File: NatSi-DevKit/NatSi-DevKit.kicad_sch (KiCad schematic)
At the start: 42 parts, among them J1 USB_TypeC, J2 Conn_01x22_Pin, J3 Conn_01x22_Pin, J4 MEM2067-02-180-00-A_REVB, SW1 SW_Push, SW2 SW_Push, SW3 SW_Push, U1 USBLC6-2SC6, U2 ESP32-S3-WROOM-1, U3 NCP1117-3.3_SOT223

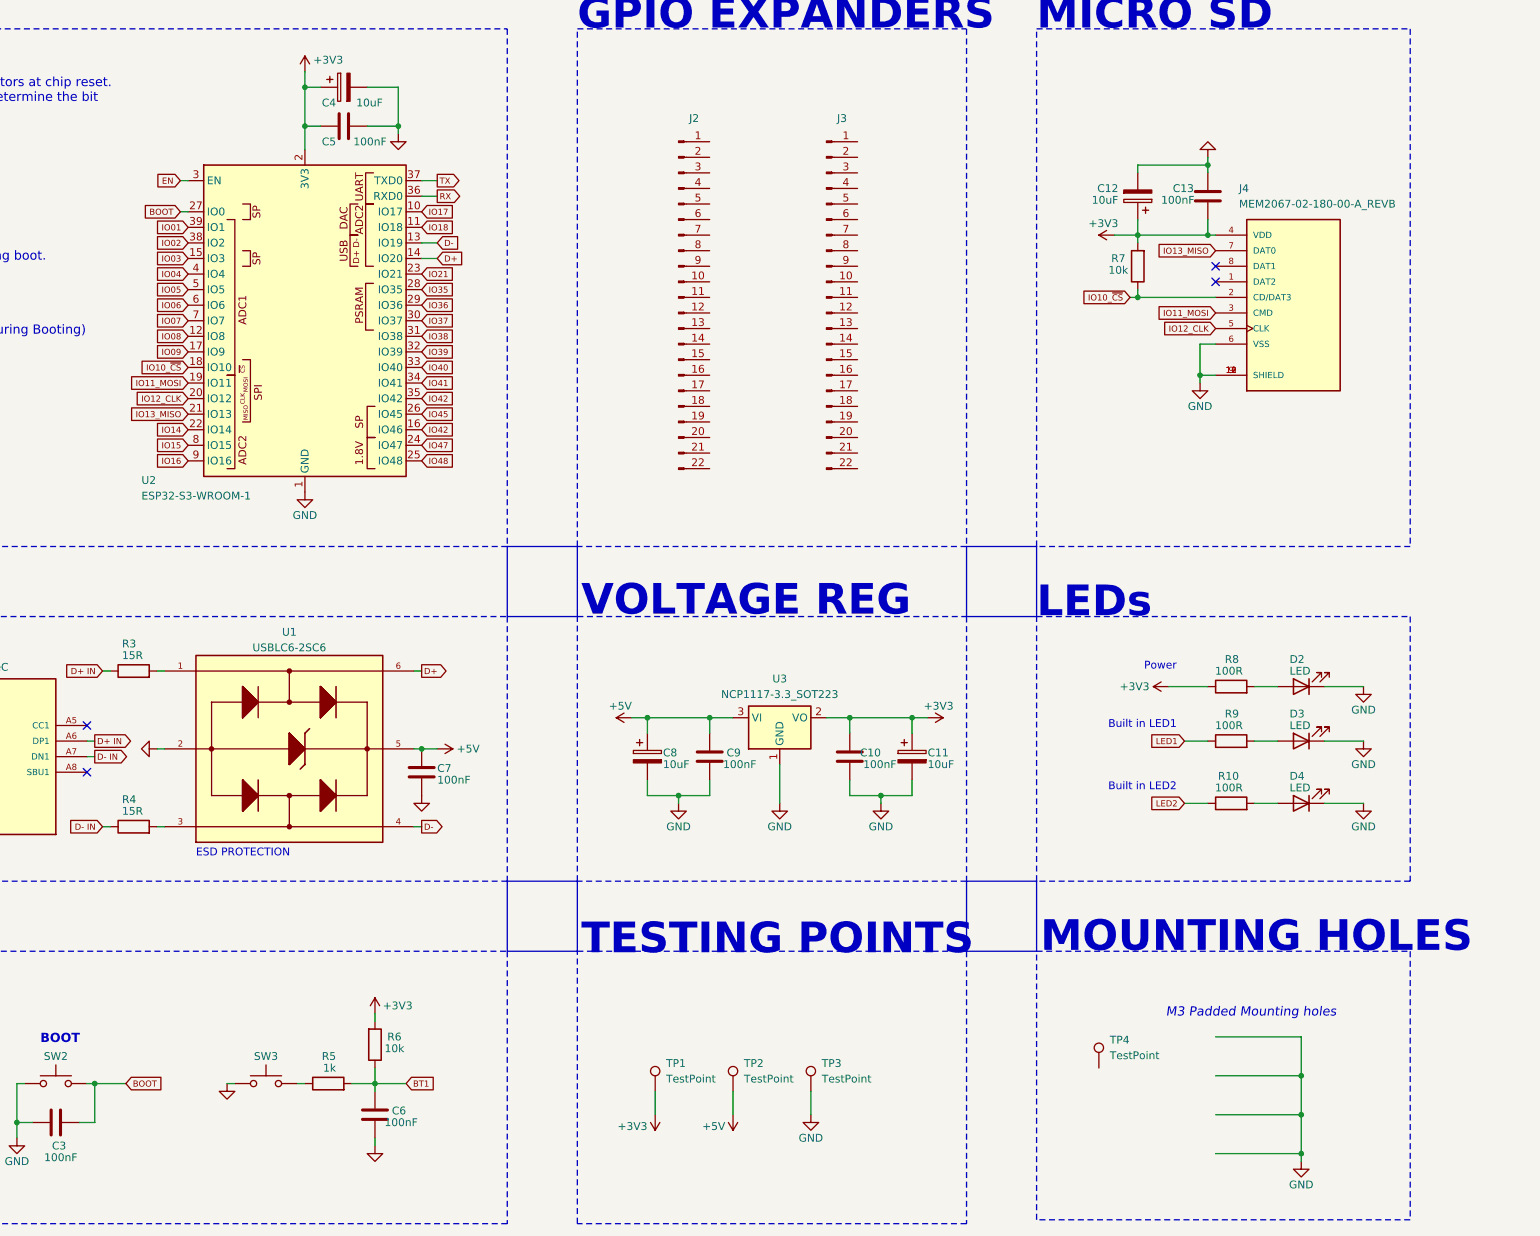
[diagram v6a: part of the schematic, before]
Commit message: PCB routing update
fuuyah a lot of pain to do these routes, Im also a shitty person.
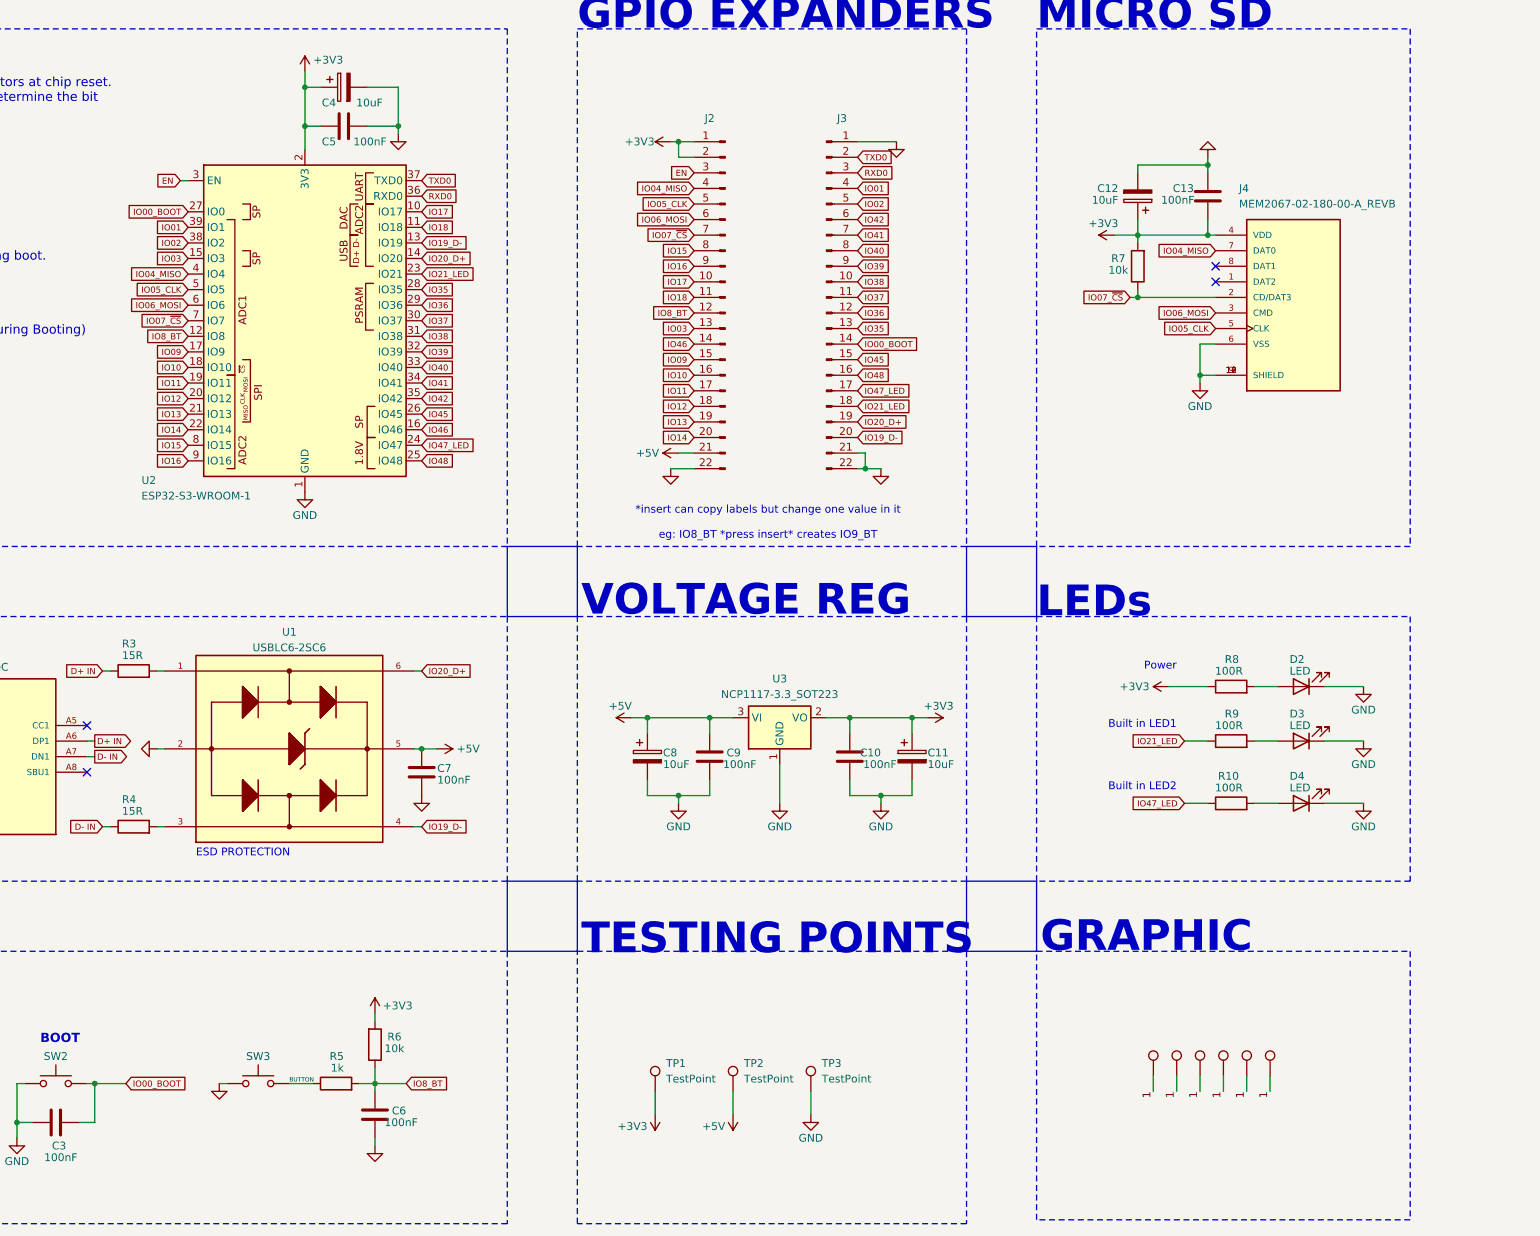
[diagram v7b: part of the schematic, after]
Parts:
- added TP5: TestPoint, sumec_graphic:NAT_PFP_IMG, symbol Connector:TestPoint
- added TP6: TestPoint, sumec_graphic:FLO_FRONT_C_IMG, symbol Connector:TestPoint
- added TP7: TestPoint, sumec_graphic:LIVE_NAT_REACTION_NEG, symbol Connector:TestPoint
- added TP8: TestPoint, sumec_graphic:FLO_SLEEP_IMG, symbol Connector:TestPoint
- added TP9: TestPoint, sumec_graphic:FLO_POINTING_IMG, symbol Connector:TestPoint
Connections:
- net BOOT is gone; now on net IO00_BOOT: C3.1, SW2.2, U2.27 (IO0)
- net BT1 is gone; now on net IO8_BT: C6.2, R5.2, R6.1
- net D+ is gone; now on net IO20_D+: U1.6, U2.14 (IO20)
- net D- is gone; now on net IO19_D-: U1.4, U2.13 (IO19)
- net IO04 is gone; now on net IO04_MISO: U2.4 (IO4)
- net IO05 is gone; now on net IO05_CLK: U2.5 (IO5)
- net IO06 is gone; now on net IO06_MOSI: U2.6 (IO6)
- net IO07 is gone; now on net IO07_~{CS}: U2.7 (IO7)
- net IO08 is gone; now on net IO8_BT: U2.12 (IO8)
- net IO21 is gone; now on net IO21_LED: U2.23 (IO21)
- net IO47 is gone; now on net IO47_LED: U2.24 (IO47)
- net LED1 is gone; now on net IO21_LED: R9.1
- net LED2 is gone; now on net IO47_LED: R10.1
- net RX is gone; now on net RXD0: U2.36 (RXD0)
- net TX is gone; now on net TXD0: U2.37 (TXD0)
- net +3V3: now also J2.1 (Pin_1), J2.2 (Pin_2)
- net +5V: now also J2.21 (Pin_21)
- net EN: now also J2.3 (Pin_3)
- net GND: now also J2.22 (Pin_22), J3.1 (Pin_1), J3.21 (Pin_21), J3.22 (Pin_22)
- net IO01: now also J3.4 (Pin_4)
- net IO02: now also J3.5 (Pin_5)
- net IO03: now also J2.13 (Pin_13)
- net IO09: now also J2.15 (Pin_15)
- net IO14: now also J2.20 (Pin_20)
- net IO15: now also J2.8 (Pin_8)
- net IO16: now also J2.9 (Pin_9)
- net IO17: now also J2.10 (Pin_10)
- net IO18: now also J2.11 (Pin_11)
- net IO35: now also J3.13 (Pin_13)
- net IO36: now also J3.12 (Pin_12)
- net IO37: now also J3.11 (Pin_11)
- net IO38: now also J3.10 (Pin_10)
- net IO39: now also J3.9 (Pin_9)
- net IO40: now also J3.8 (Pin_8)
- net IO41: now also J3.7 (Pin_7)
- net IO42: now also J3.6 (Pin_6); no longer U2.16 (IO46)
- net IO45: now also J3.15 (Pin_15)
- net IO48: now also J3.16 (Pin_16)
- net BUTTON: now reaches R5.1, SW3.2
- net IO8_BT: now reaches J2.12 (Pin_12)
- net IO46: now reaches J2.14 (Pin_14)
- net IO46: now also U2.16 (IO46)
- net IO10: now reaches J2.16 (Pin_16)
- net IO10: now also U2.18 (IO10)
- net IO11: now reaches J2.17 (Pin_17)
- net IO11: now also U2.19 (IO11)
- net IO12: now reaches J2.18 (Pin_18)
- net IO12: now also U2.20 (IO12)
- net IO13: now reaches J2.19 (Pin_19)
- net IO13: now also U2.21 (IO13)
- net IO04_MISO: now reaches J2.4 (Pin_4)
- net IO04_MISO: now also J4.7 (DAT0)
- net IO05_CLK: now reaches J2.5 (Pin_5)
- net IO05_CLK: now also J4.5 (CLK)
- net IO06_MOSI: now reaches J2.6 (Pin_6)
- net IO06_MOSI: now also J4.3 (CMD)
- net IO07_~{CS}: now reaches J2.7 (Pin_7)
- net IO07_~{CS}: now also J4.2 (CD/DAT3), R7.1
- net 1: now reaches TP4.1
- net 1: now also TP5.1, TP6.1, TP7.1, TP8.1, TP9.1
- net IO00_BOOT: now reaches J3.14 (Pin_14)
- net IO47_LED: now reaches J3.17 (Pin_17)
- net IO21_LED: now reaches J3.18 (Pin_18)
- net IO20_D+: now reaches J3.19 (Pin_19)
- net TXD0: now reaches J3.2 (Pin_2)
- net IO19_D-: now reaches J3.20 (Pin_20)
- net RXD0: now reaches J3.3 (Pin_3)
- removed net IO10_~{CS}: J4.2 (CD/DAT3), R7.1, U2.18 (IO10)
- removed net IO11_MOSI: J4.3 (CMD), U2.19 (IO11)
- removed net IO12_CLK: J4.5 (CLK), U2.20 (IO12)
- removed net IO13_MISO: J4.7 (DAT0), U2.21 (IO13)
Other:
- note added: "*insert can copy labels but change one value in it eg: IO8_BT *press insert* creates IO9_BT"
- note added: "GRAPHIC"
- note removed: "M3 Padded Mounting holes"
- note removed: "MOUNTING HOLES"
- moved on the sheet: J2, R5, SW3

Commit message: some 3d updates
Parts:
- SW1, SW2, SW3: footprint Button_Switch_SMD:SW_SPST_EVQPE1 -> sumec_brd:SW_SPST_EVQPE1
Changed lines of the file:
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@@
 			)
 		)
-		(property "Footprint" "Button_Switch_SMD:SW_SPST_EVQPE1"
+		(property "Footprint" "sumec_brd:SW_SPST_EVQPE1"
 			(at 179.07 215.9 0)
 			(effects
@@
 			)
 		)
-		(property "Footprint" "Button_Switch_SMD:SW_SPST_EVQPE1"
+		(property "Footprint" "sumec_brd:SW_SPST_EVQPE1"
 			(at 146.05 215.9 0)
 			(effects
@@
 			)
 		)
-		(property "Footprint" "Button_Switch_SMD:SW_SPST_EVQPE1"
+		(property "Footprint" "sumec_brd:SW_SPST_EVQPE1"
 			(at 123.19 215.9 0)
 			(effects
